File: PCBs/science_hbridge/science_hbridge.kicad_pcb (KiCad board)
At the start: 2 copper layers, 47.5 x 47.1 mm, 34 parts, among them J1 Conn_02x07_Odd_Even, J2 Conn_02x08_Odd_Even, J3 Conn_02x08_Odd_Even, J4 Conn_01x06, J6 Conn_01x02_Pin, J7 Conn_01x04_Pin, J8 Conn_01x06, U1 L298N, U2 MAX485E, U3 NCP718xSN500

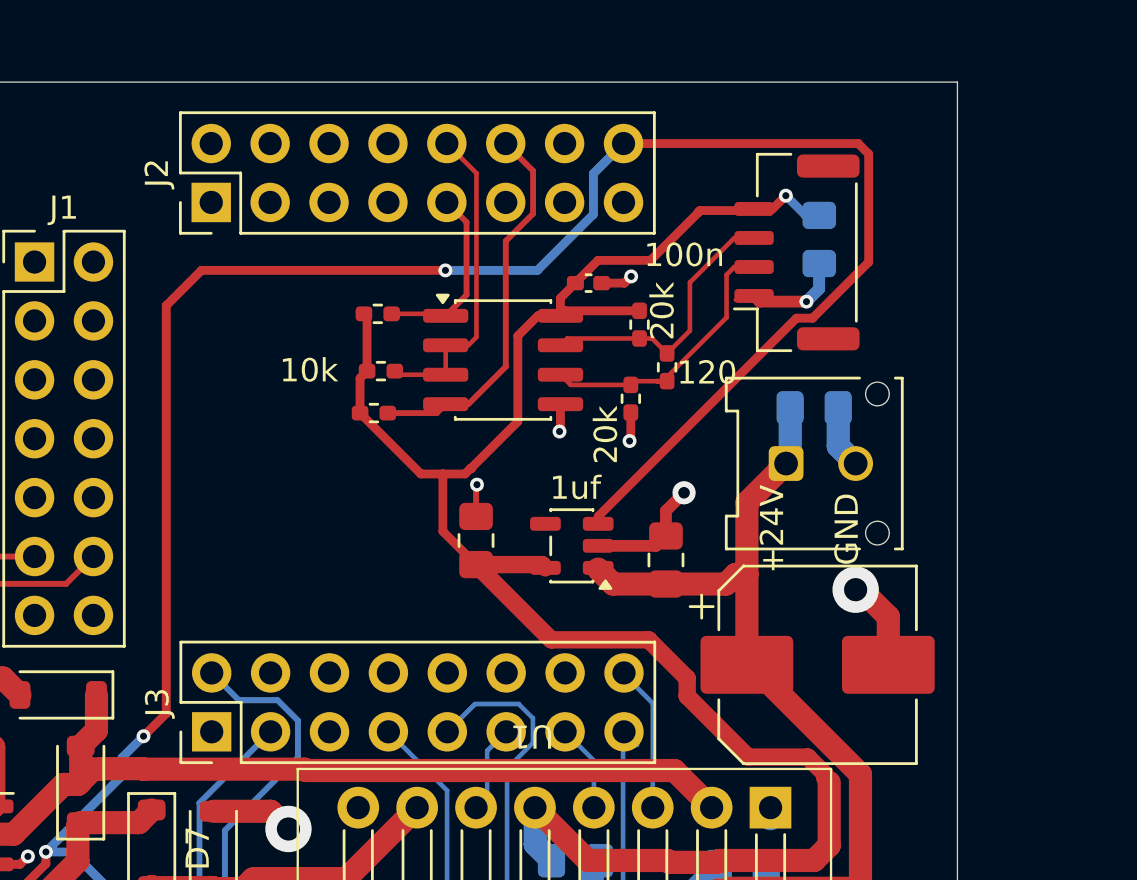
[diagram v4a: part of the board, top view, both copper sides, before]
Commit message: fixed 3.3V, fized header
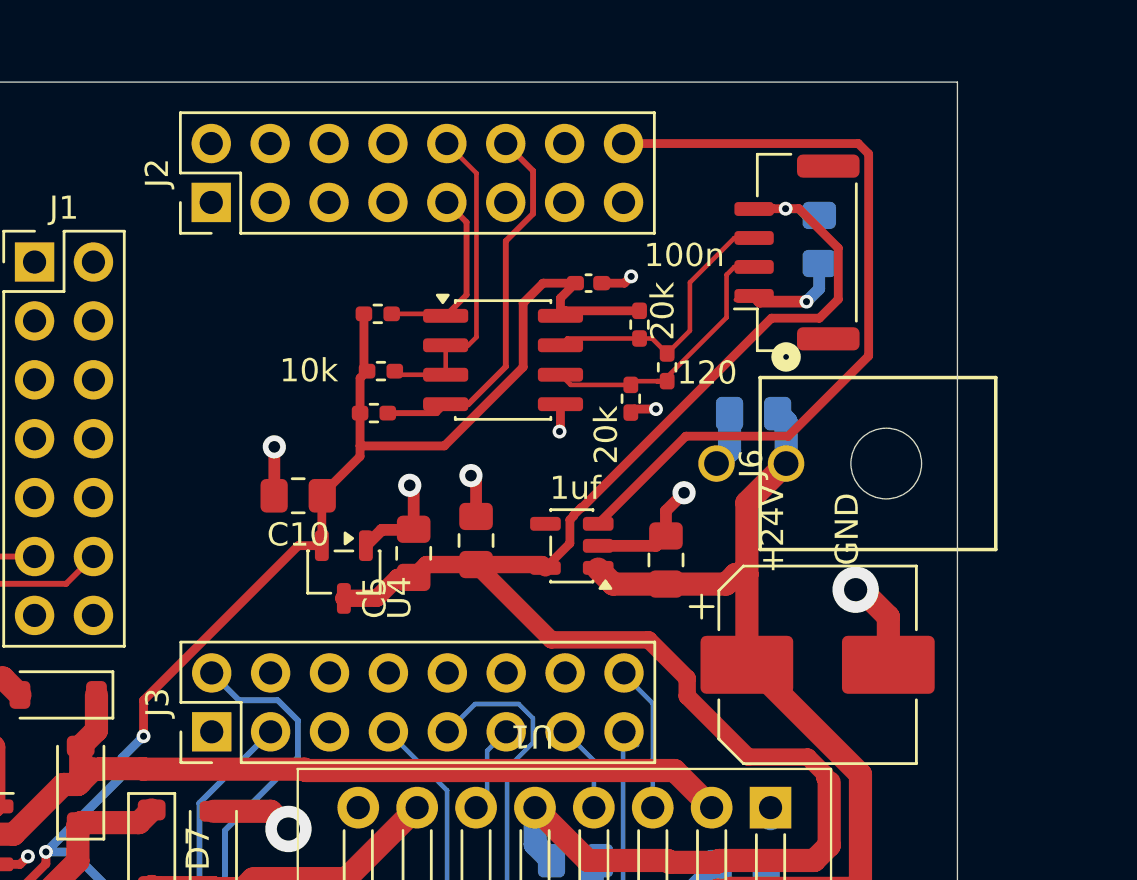
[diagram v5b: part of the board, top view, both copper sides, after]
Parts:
- added C10: 100nf, Capacitor_SMD:C_0805_2012Metric_Pad1.18x1.45mm_HandSolder, F.Cu at (137.6, 69.3)
- added C5: 100nf, Capacitor_SMD:C_0805_2012Metric_Pad1.18x1.45mm_HandSolder, F.Cu at (142.6, 71.8)
- added U4: XC6206PxxxMR, Package_TO_SOT_SMD:SOT-23-3, F.Cu at (139.6, 72.6)
- J6: footprint Connector_Molex:Molex_Micro-Fit_3.0_43045-0212_2x01_P3.00mm_Vertical -> footprints:CONN_SD-43045-001_02_MOL
- moved C9 2.62 mm to (157.3, 65.8), turned to 180 degrees
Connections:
- C4 pad 1: +5V -> +3.3V
- R10 pad 1: +5V -> +3.3V
- R12 pad 1: +5V -> +3.3V
- R14 pad 1: +5V -> +3.3V
- R7 pad 1: +5V -> +3.3V
- U2 pad 8: +5V -> +3.3V
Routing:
- net +5V: track 83.3 -> 74.6 mm
- net GND: track 39.6 -> 46.0 mm, vias 11 -> 13
- net +3.3V: track 94.3 -> 95.8 mm, vias 4 -> 3
